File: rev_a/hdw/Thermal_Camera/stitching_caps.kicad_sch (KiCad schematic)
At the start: 16 parts

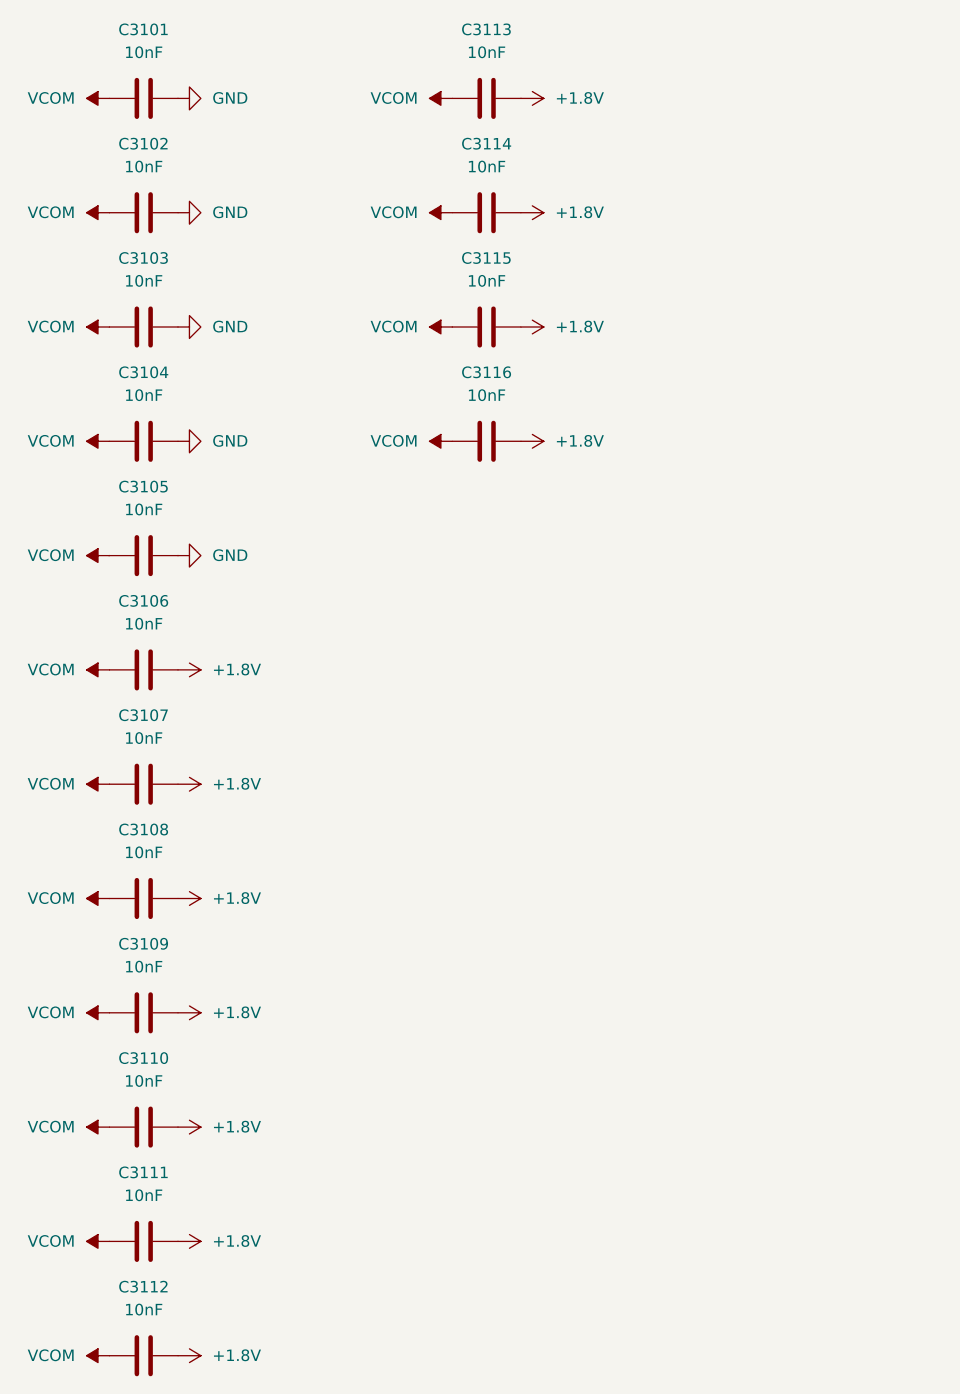
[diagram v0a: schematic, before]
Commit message: added some more stitching caps
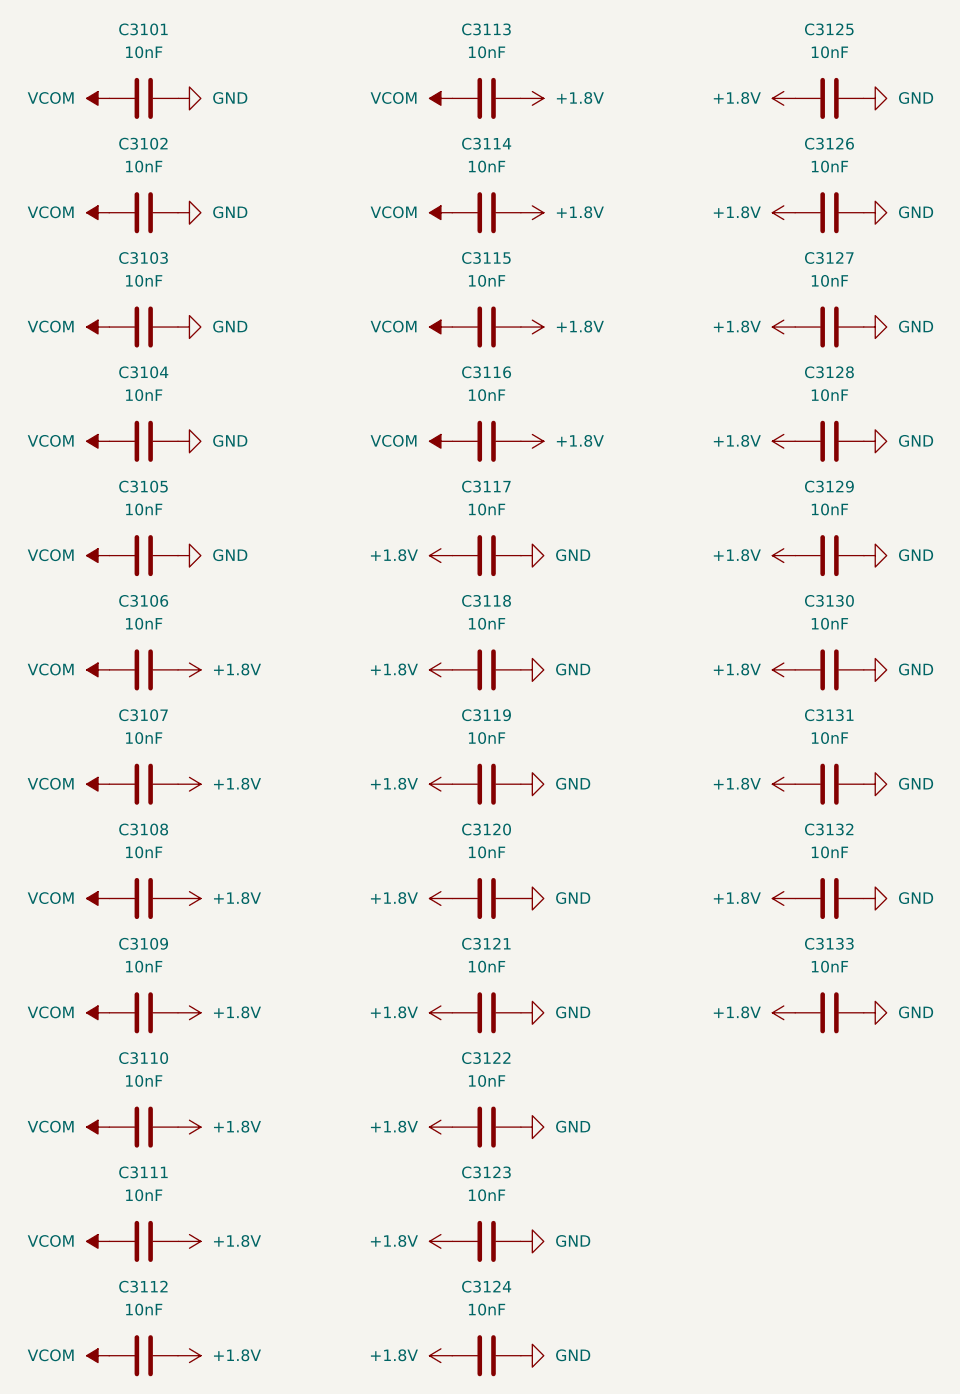
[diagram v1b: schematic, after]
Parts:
- added C3117, C3118, C3119, C3120, C3121, C3122, C3123, C3124, C3125, C3126, C3127, C3128, C3129, C3130, C3131, C3132, C3133: 10nF, Capacitors_SMD:C_0402, symbol Custom_Library:C_Custom
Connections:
- net +1.8V: now also C3117.1, C3118.1, C3119.1, C3120.1, C3121.1, C3122.1, C3123.1, C3124.1, C3125.1, C3126.1, C3127.1, C3128.1, C3129.1, C3130.1, C3131.1, C3132.1, C3133.1
- net GND: now also C3117.2, C3118.2, C3119.2, C3120.2, C3121.2, C3122.2, C3123.2, C3124.2, C3125.2, C3126.2, C3127.2, C3128.2, C3129.2, C3130.2, C3131.2, C3132.2, C3133.2
